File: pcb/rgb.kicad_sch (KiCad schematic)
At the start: 37 parts, among them J1 2.54-2*8P, J3 B4PS-VH, J4 TYPE-C-31-M-12, J5 TF-01A, J7 B4PS-VH, SW1 MS-22C01-G010, U4 EVQQ2, U5 ESP32-WROOM-32E, U7 CH340C, U8 SPX3819M5-L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

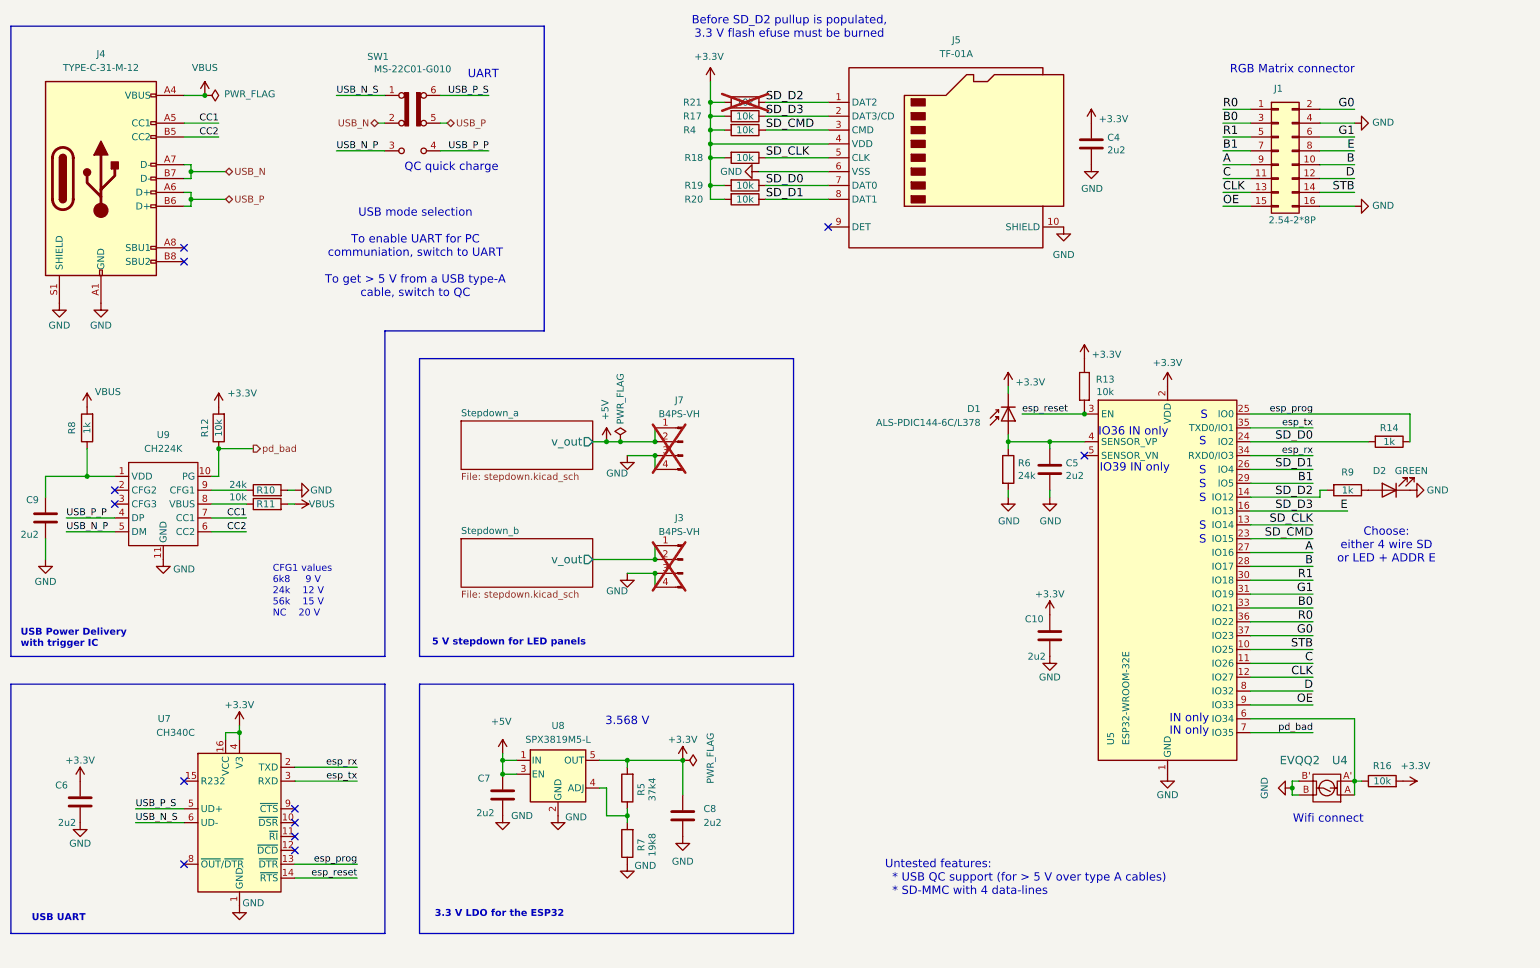
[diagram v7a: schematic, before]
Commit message: schematic: add jumper resistors to isolate SD card and panel pins
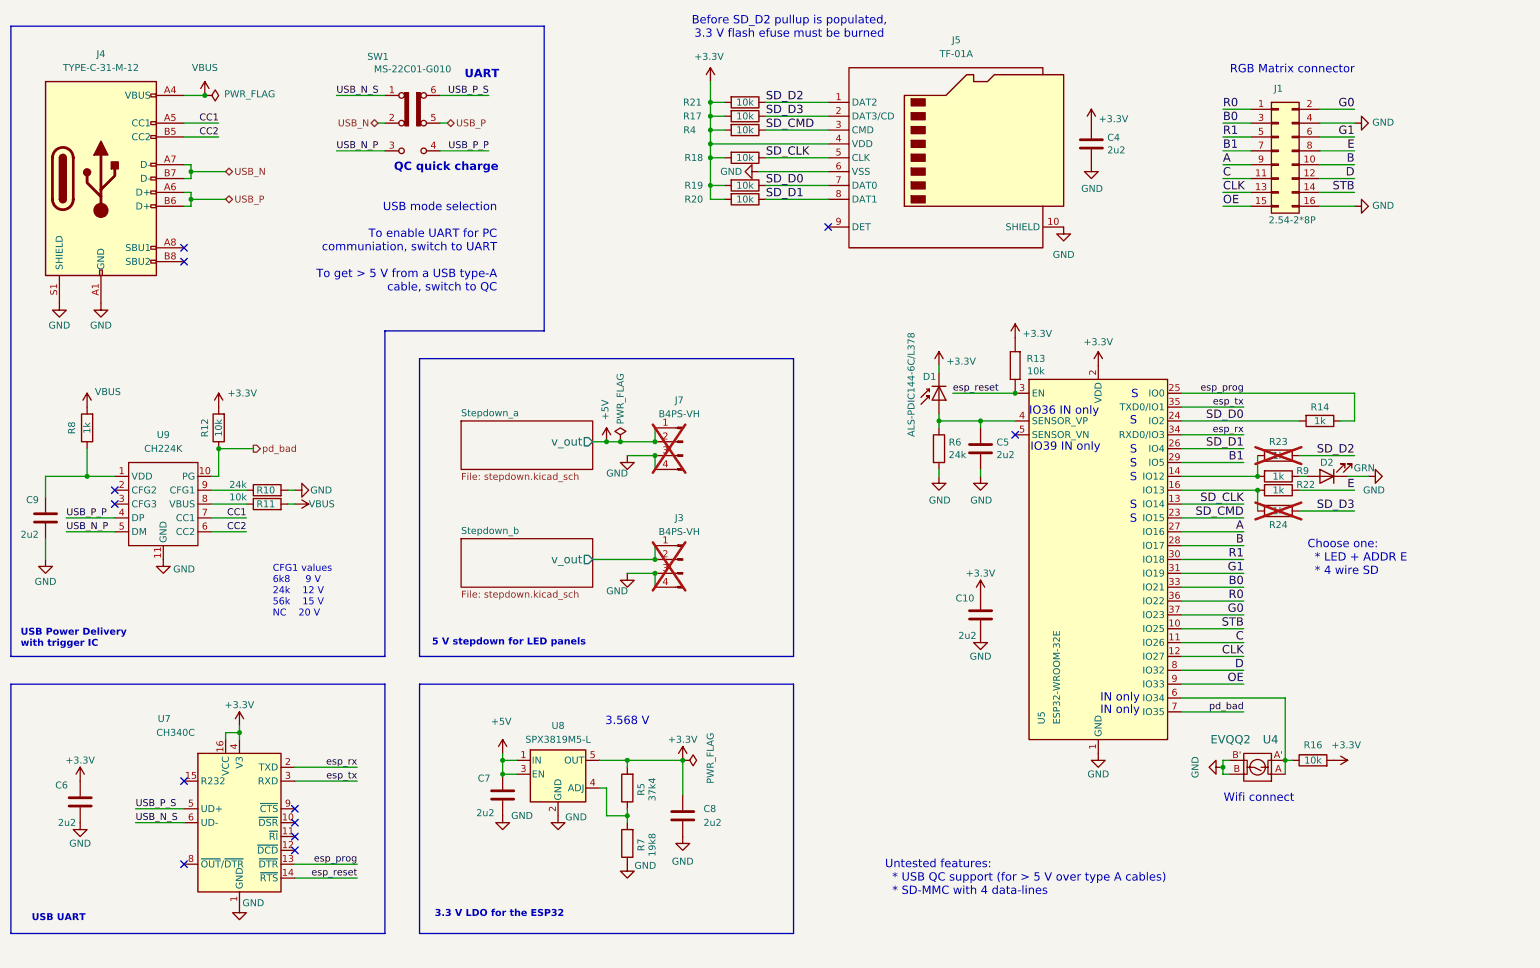
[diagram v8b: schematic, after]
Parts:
- added R22, R23, R24: 1k, Resistor_SMD:R_0603_1608Metric, symbol Device:R
- D2: value GREEN -> GRN
- R21: now fitted
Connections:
- net E: now also R22.1; no longer J5.2 (DAT3/CD), R17.1, U5.16 (IO13)
- net SD_D2: now also R23.1; no longer R9.2, U5.14 (IO12)
- new net: R22.2, R24.2, U5.16 (IO13)
- new net: R23.2, R9.2, U5.14 (IO12)
- new net SD_D3: J5.2 (DAT3/CD), R17.1, R24.1
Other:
- note added: "Choose one: * LED + ADDR E * 4 wire SD"
- note removed: "Choose: either 4 wire SD or LED + ADDR E"
- moved on the sheet: C10, C5, D1, D2, R13, R14, R16, R6, R9, U4, U5
